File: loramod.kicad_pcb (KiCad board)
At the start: 2 copper layers, 50 x 30 mm, 78 parts, among them P1 CONN_02X08, P2 ANT, U1 TXEABDSANF-32, U2 LD3985G30R, U3 SX1276, U4 PE42421, U5 MAAL-010704, U6 MMZ09312BT1

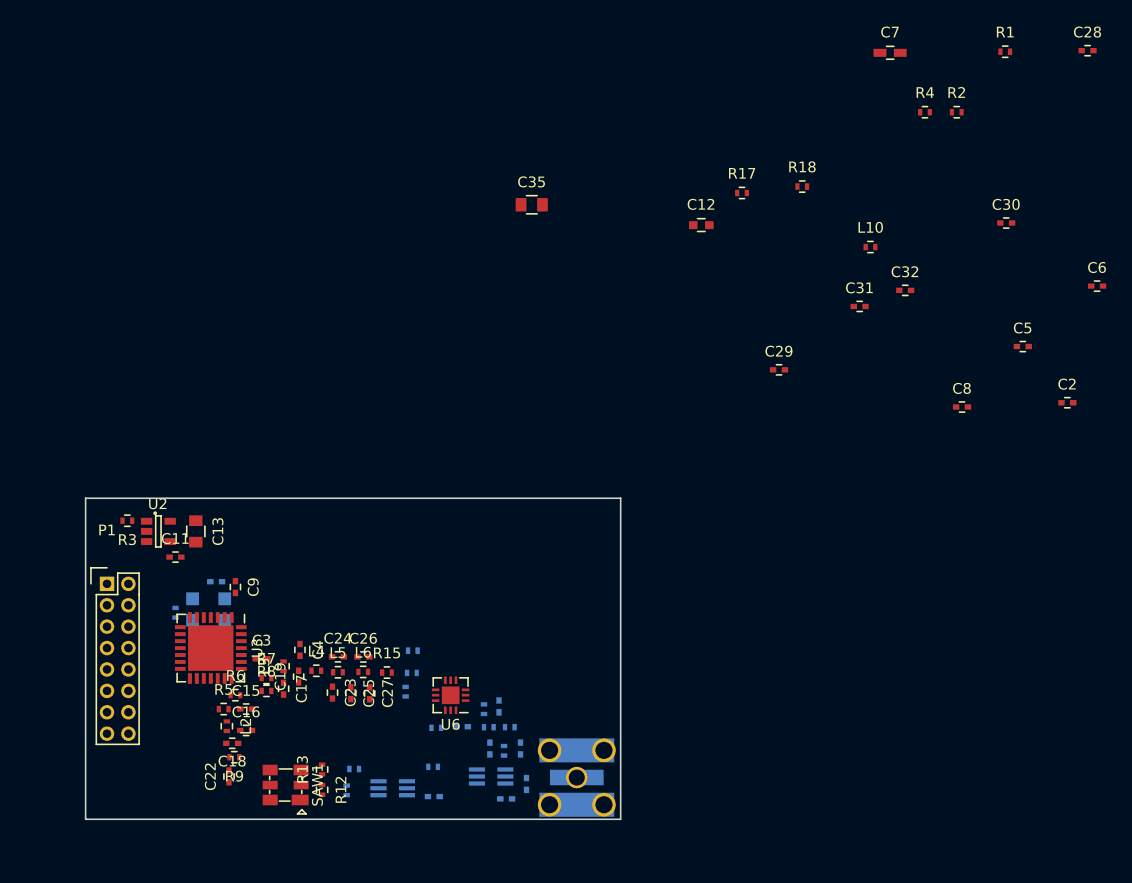
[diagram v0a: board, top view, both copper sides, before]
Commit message: PCB part placement done
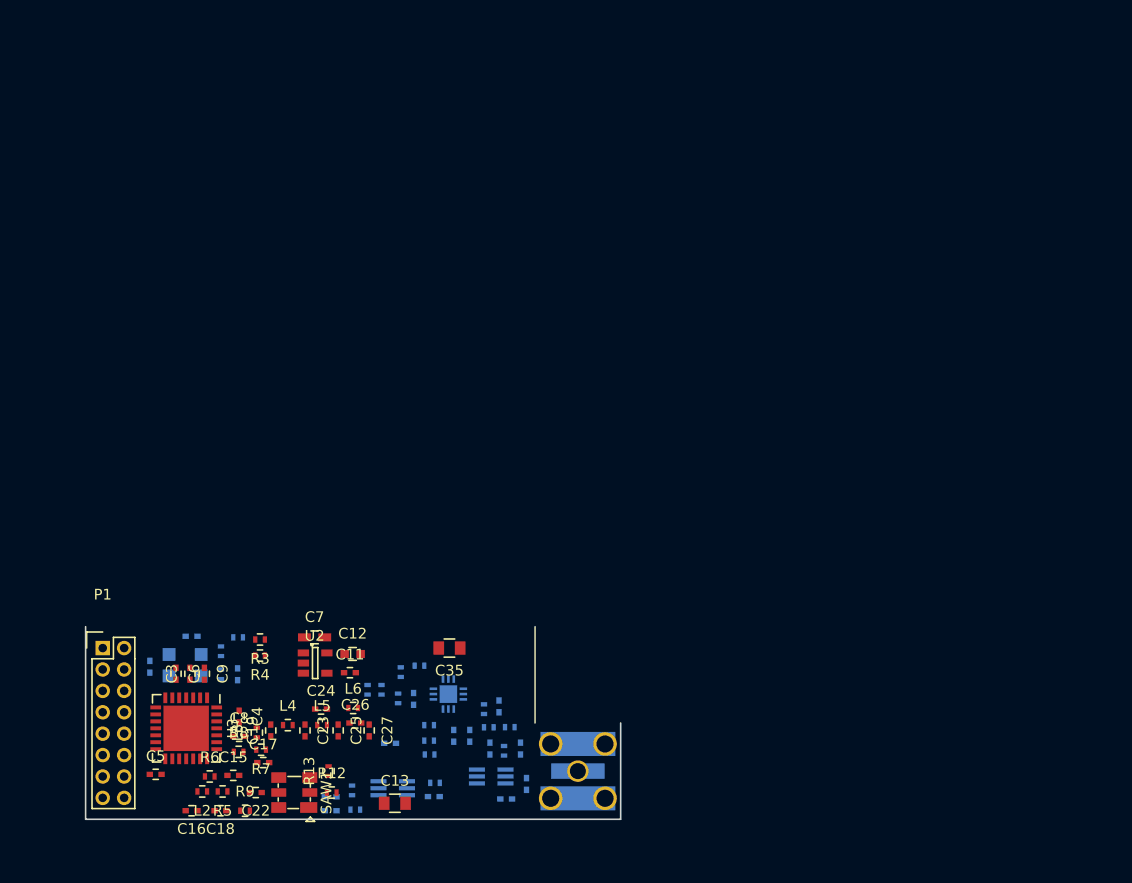
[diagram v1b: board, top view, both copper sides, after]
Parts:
- C2, C28, C29, C30, C31, C32, L10, R1, R15, R17, R18, R2, U6: moved to B.Cu
- moved C28 99.3 mm to (172.9, 77.9), turned to 180 degrees
- moved C6 93.4 mm to (158.4, 66.4), turned to 270 degrees
- moved R1 92.2 mm to (162.7, 64.3), turned to 270 degrees
- moved C5 90.4 mm to (156.6, 75.8)
- moved R2 86.5 mm to (162.7, 66.5), turned to 270 degrees
- moved C2 84.7 mm to (159.9, 62.9), turned to 180 degrees
- moved R4 80.2 mm to (166.3, 64.7), turned to 180 degrees
- moved C7 76.7 mm to (171.4, 63.0)
- moved C8 74.2 mm to (164.3, 72.2)
- moved C30 71.0 mm to (180.7, 68.8), turned to 270 degrees
- moved L10 61.9 mm to (182.1, 72.7)
- moved R18 61.2 mm to (182.1, 71.2)
- moved C31 59.9 mm to (178.4, 72.9), turned to 180 degrees
- moved C32 59.3 mm to (184.4, 72.2), turned to 90 degrees
- moved C29 58.8 mm to (172.9, 79.2), turned to 180 degrees
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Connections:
- R1 pad 1: 3V0 -> Net-(C2-Pad1)
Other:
- board size 50 x 30 mm -> 50 x 18 mm

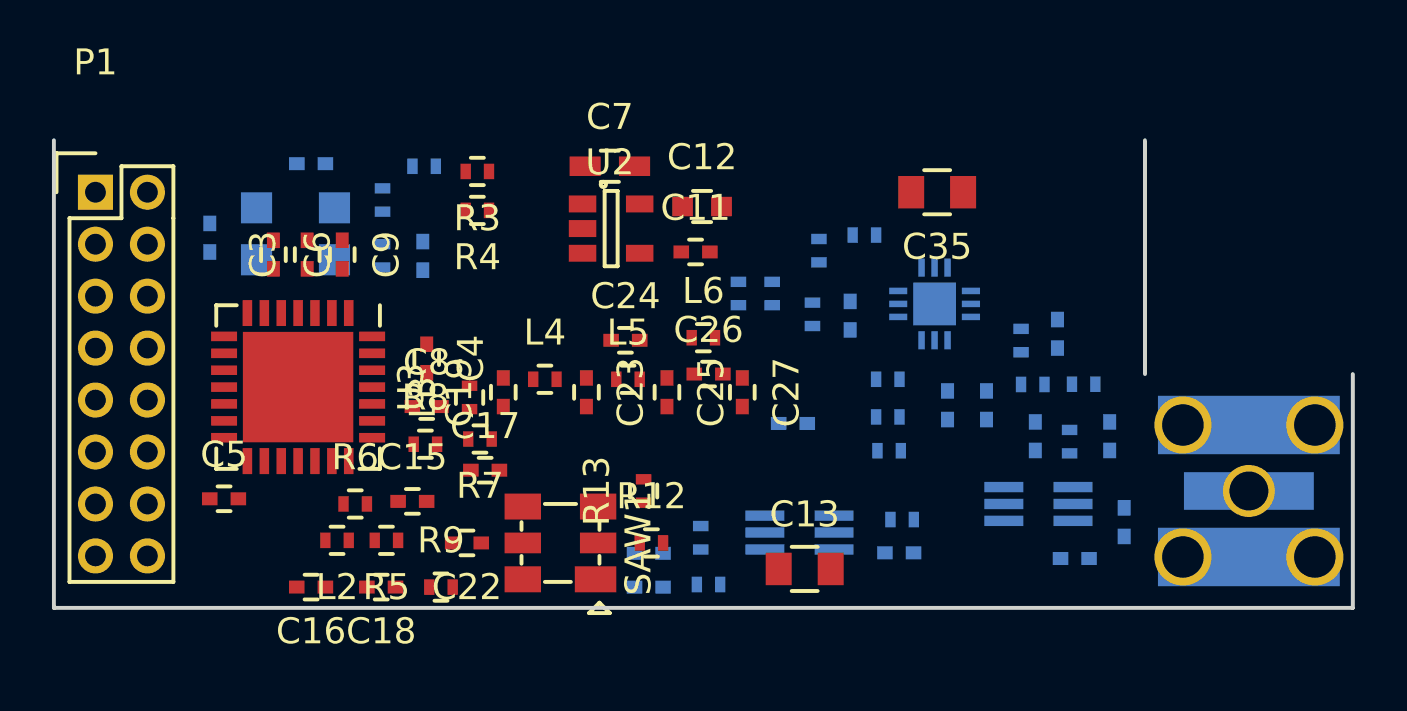
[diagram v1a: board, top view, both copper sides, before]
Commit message: All tracks routed, need to create ground planes
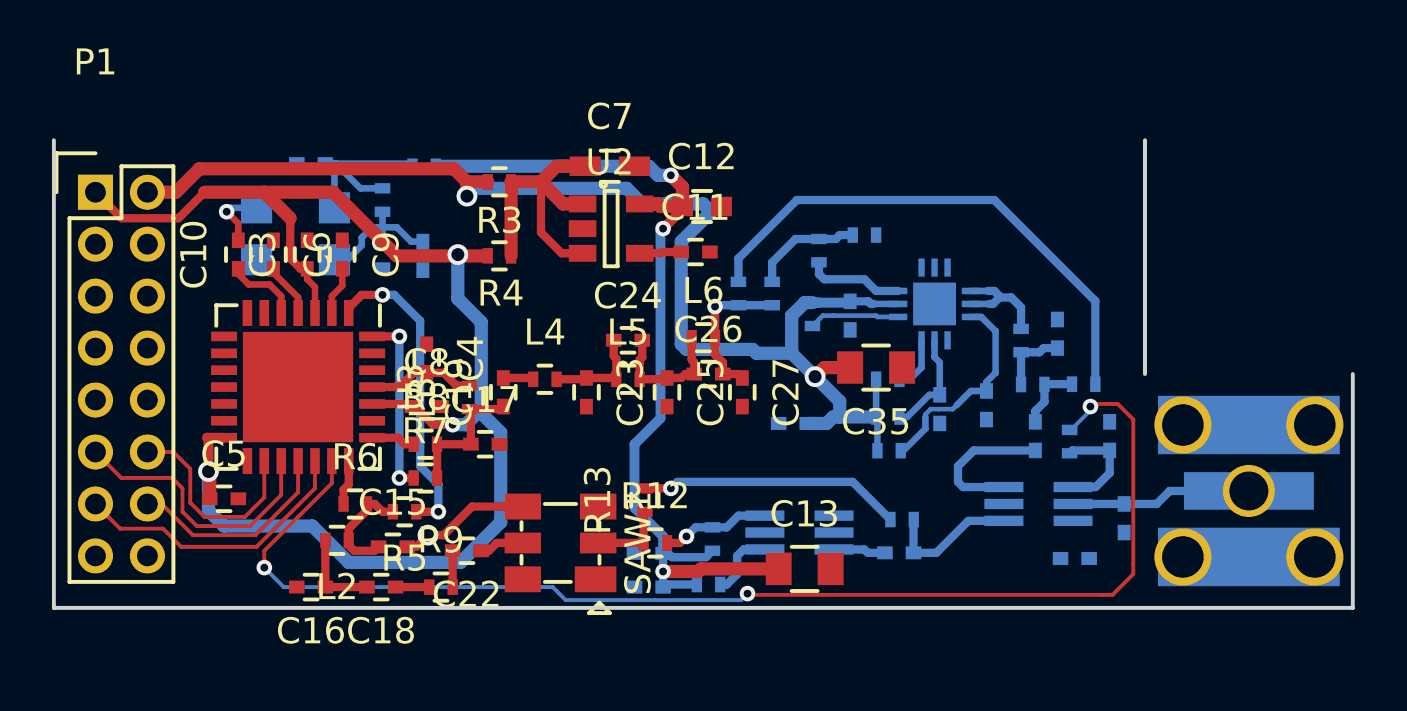
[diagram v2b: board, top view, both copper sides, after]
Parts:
- C10: moved to F.Cu
- moved C35 7.15 mm to (181.7, 70.8)
- moved R7 2.58 mm to (164.3, 75.0), turned to 0 degrees
- moved R4 1.95 mm to (167.2, 66.5)
- moved C15 1.90 mm to (163.1, 77.7)
- moved R5 1.30 mm to (163.5, 76.3)
- moved C10 1.28 mm to (157.1, 66.4)
- moved C17 1.00 mm to (166.6, 73.7)
- moved R3 0.94 mm to (167.2, 63.6)
- moved L7 0.45 mm to (175.3, 77.3)
- moved R13 0.35 mm to (172.8, 75.8)
- moved C32 0.34 mm to (184.1, 72.3)
- moved C22 0.30 mm to (165.9, 77.8)
- moved D1 0.15 mm to (191.2, 76.5)
- moved R12 0.15 mm to (173.2, 77.5)
- moved C24 0.10 mm to (172.1, 69.7)
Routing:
- net VCC: track 0.00 -> 55.7 mm, vias 0 -> 3
- net +5V: track 0.00 -> 50.2 mm, vias 0 -> 2
- net /SW_CTRL: track 0.00 -> 48.8 mm, vias 0 -> 3
- net 3V0: track 0.00 -> 36.0 mm, vias 0 -> 3
- net Net-(R14-Pad2): track 0.00 -> 20.4 mm
- net /RFI_LF: track 0.00 -> 12.4 mm, vias 0 -> 2
- net Net-(C7-Pad1): track 0.00 -> 11.8 mm
- net /LORA_~CS: track 0.00 -> 11.1 mm
- net /LORA_MISO: track 0.00 -> 10.7 mm
- net Net-(R13-Pad2): track 0.00 -> 10.2 mm, vias 0 -> 1
- net Net-(C36-Pad2): track 0.00 -> 8.20 mm
- net /LORA_MOSI: track 0.00 -> 8.18 mm
- net /LORA_SCK: track 0.00 -> 8.01 mm
- net Net-(C2-Pad1): track 0.00 -> 7.83 mm
- net /RFO_LF: track 0.00 -> 7.05 mm, vias 0 -> 2
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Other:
- copper layers 2 -> 4
- net class Default: clearance 0.2 -> 0.15; trace_width 0.25 -> 0.15; via_drill 0.4 -> 0.3
- rule trace_clearance: 0.2 -> 0.15
- rule trace_min: 0.2 -> 0.15
- rule via_min_size: 0.4 -> 0.6

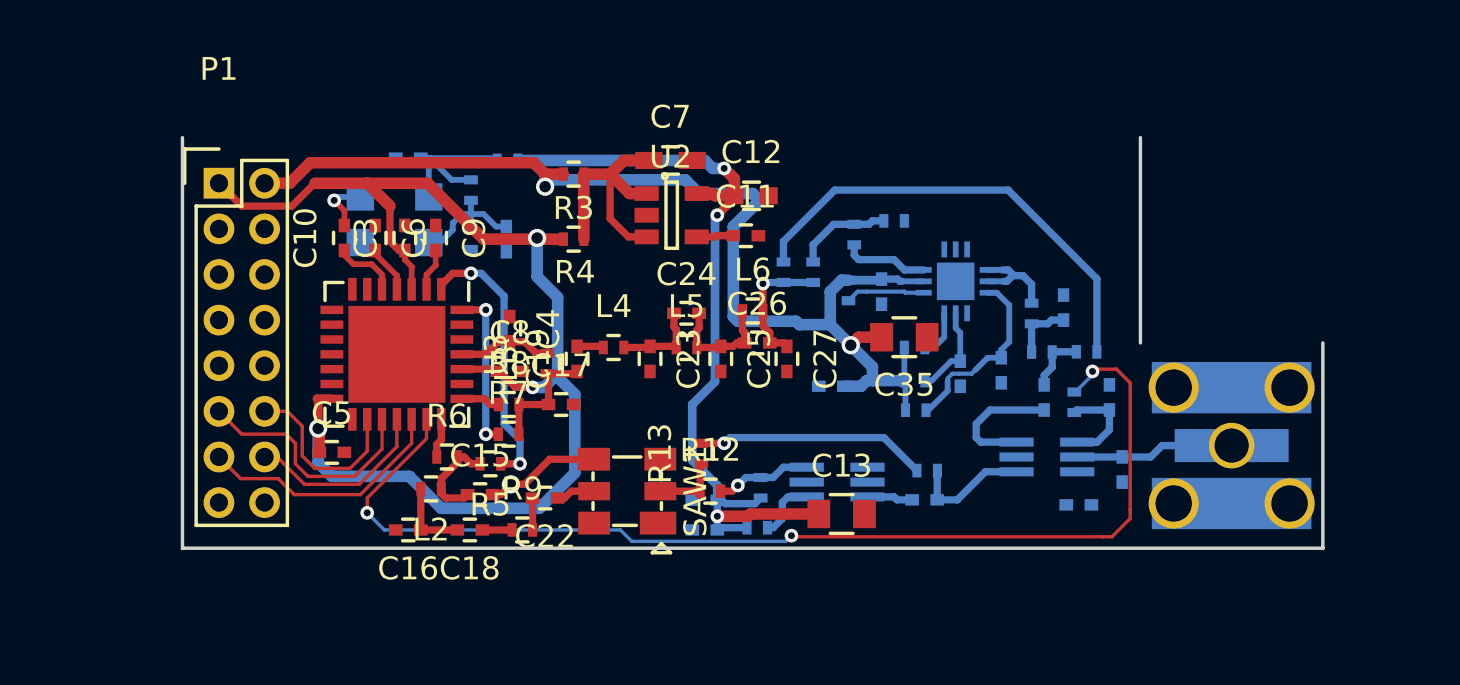
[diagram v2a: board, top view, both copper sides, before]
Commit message: Finish PCB attempt 1; add README
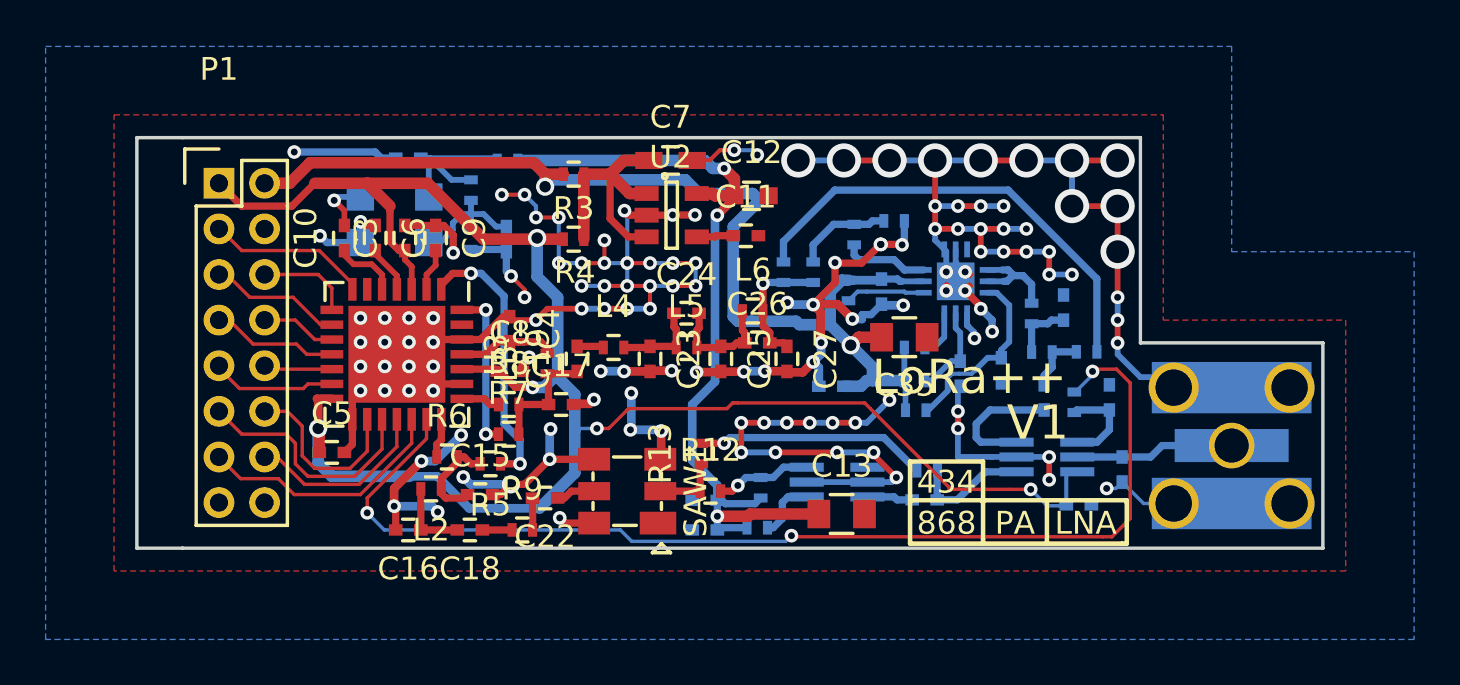
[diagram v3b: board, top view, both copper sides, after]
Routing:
- net GND: track 5.09 -> 195.2 mm, vias 1 -> 133
- net VCC: track 55.7 -> 82.1 mm, vias 3 -> 5
- net /LORA_~RST: track 0.00 -> 7.09 mm
- net /LORA_DIO1: track 0.00 -> 5.86 mm
- net /LORA_DIO3: track 0.00 -> 5.57 mm
- net /LORA_DIO5: track 0.00 -> 5.51 mm
- net /LORA_DIO0: track 0.00 -> 4.15 mm
- net /LORA_DIO2: track 0.00 -> 3.30 mm
- net /LORA_DIO4: track 0.00 -> 3.01 mm
- added copper zone on B.Cu, net GND
- added copper zone on F.Cu, net GND
- added copper zone on In1.Cu, net GND
- added copper zone on In2.Cu, net GND
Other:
- board size 50 x 18 mm -> 52 x 18 mm
- board text added: "434"
- board text added: "5V"
- board text added: "868"
- board text added: "CK"
- board text added: "D0"
- board text added: "D1"
- board text added: "D2"
- board text added: "D3"
- board text added: "D4"
- board text added: "D5"
- board text added: "G"
- board text added: "LNA"
- board text added: "LoRa++"
- board text added: "PA"
- board text added: "SI"
- board text added: "SO"
- board text added: "V1"
- board text added: "Vd"
- board text added: "~CS"
- board text added: "~R"

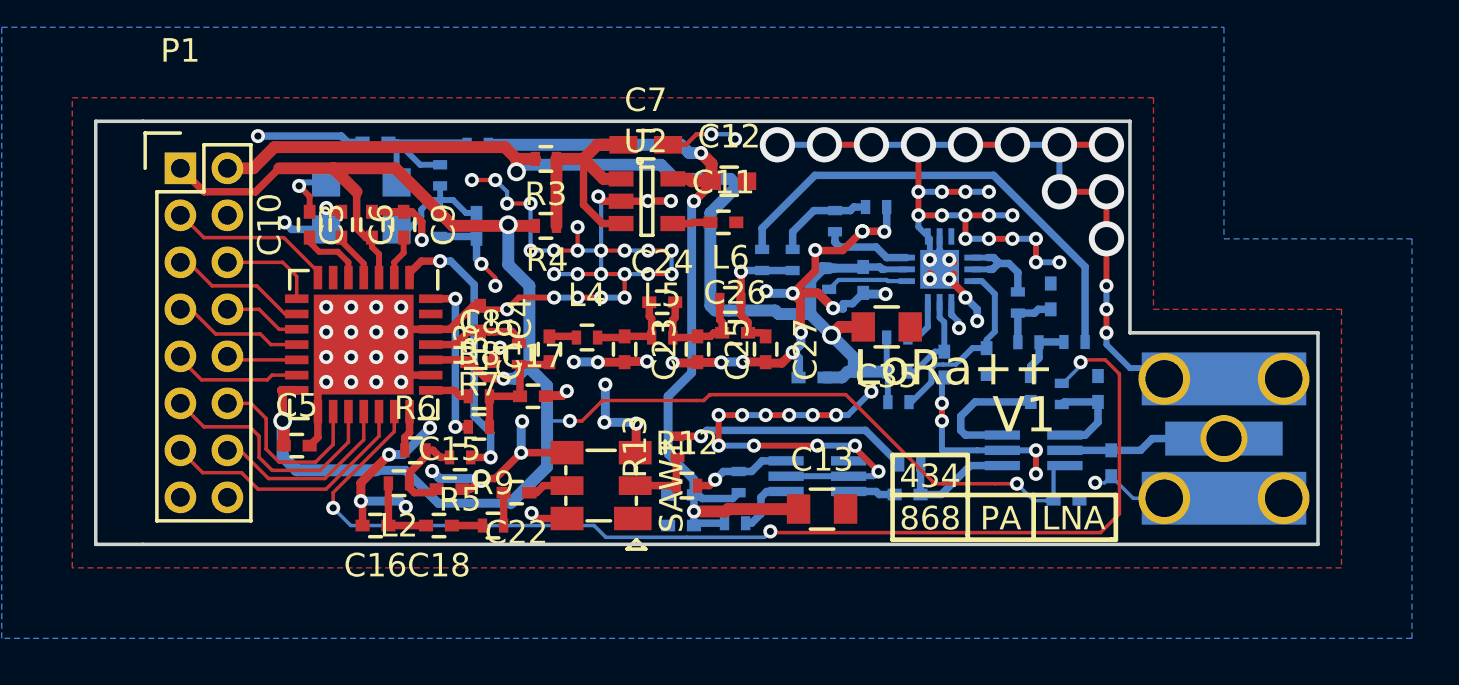
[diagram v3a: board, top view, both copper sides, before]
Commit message: Modify PCB design to fit with Elecrow's 5cm limit
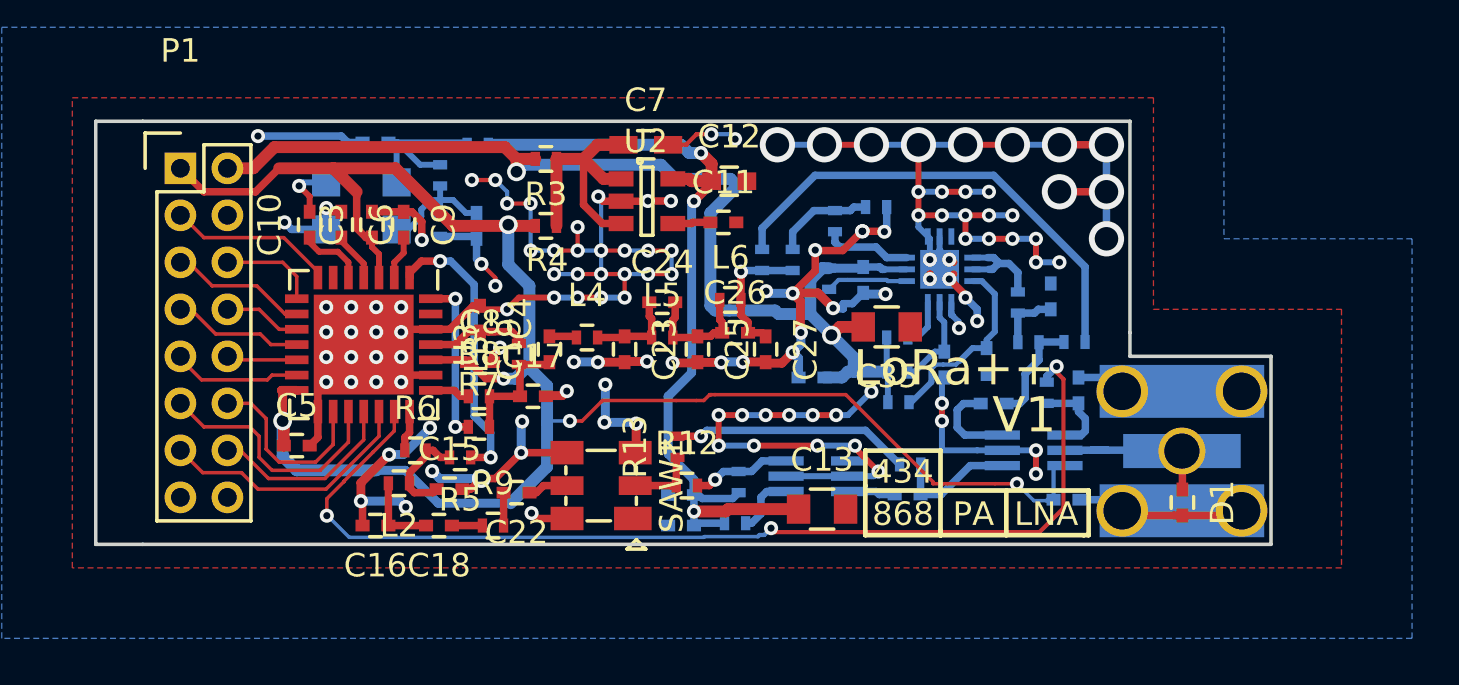
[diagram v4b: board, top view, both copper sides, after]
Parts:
- D1: moved to F.Cu
- moved D1 3.46 mm to (194.2, 78.2)
- moved P2 1.87 mm to (194.2, 76.0)
- moved C14 1.70 mm to (186.2, 74.0), turned to 0 degrees
- moved C21 0.83 mm to (189.8, 73.5)
- moved R10 0.64 mm to (188.5, 73.5)
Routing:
- net /SW_CTRL: track 48.8 -> 45.1 mm
- net /RF_OUT: track 2.65 -> 4.57 mm
- net Net-(C14-Pad1): track 5.68 -> 3.91 mm
- net GND: track 195.2 -> 194.5 mm, vias 133 -> 129
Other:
- board size 52 x 18 mm -> 50 x 18 mm
